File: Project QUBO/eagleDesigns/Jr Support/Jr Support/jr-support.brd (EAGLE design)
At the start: 242.6 x 96.8 mm, 254 parts, among them IC1 74LVC1G08DBV, IC2 TLC2272PW, IC3 74LVC1G08DBV, Q1 FDN5618P, U1 PCA9685, U2 LT3063, U3 LT3063

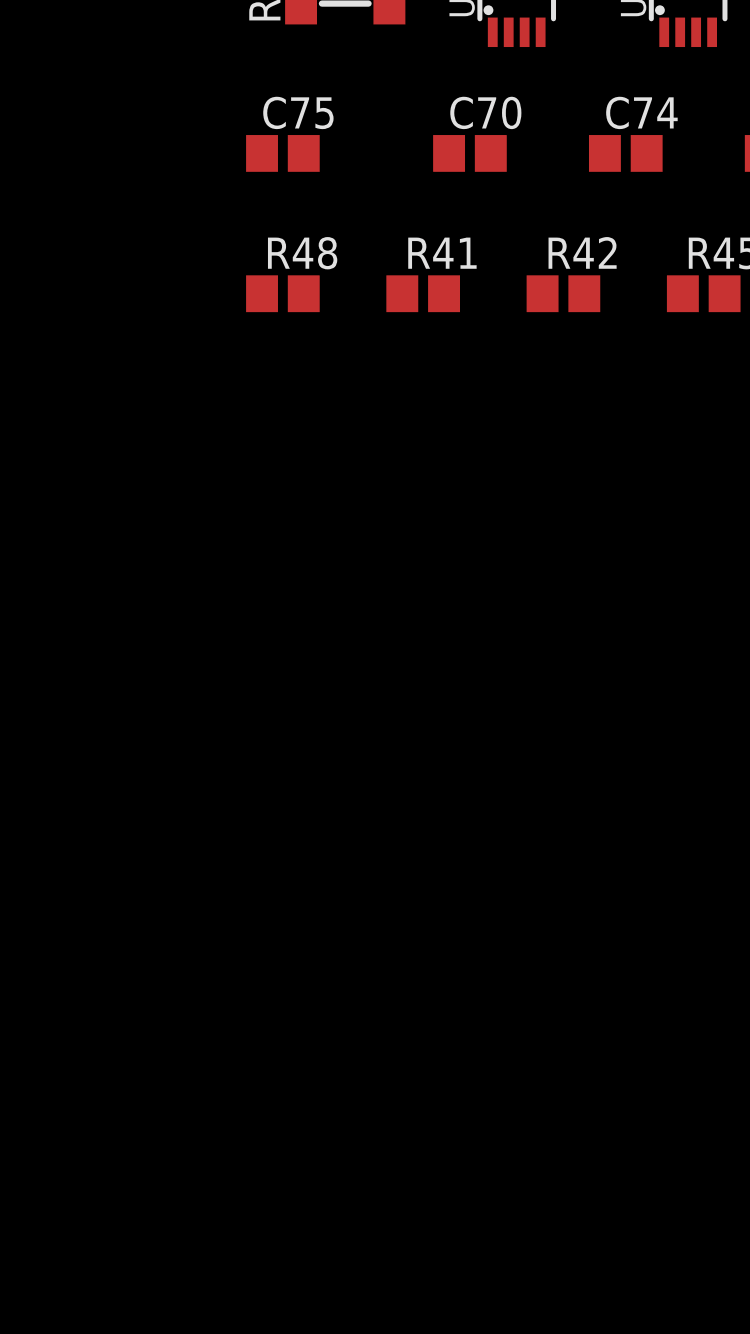
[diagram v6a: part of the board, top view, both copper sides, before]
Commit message: Created breadboards. Added 5V reg PG fault line.
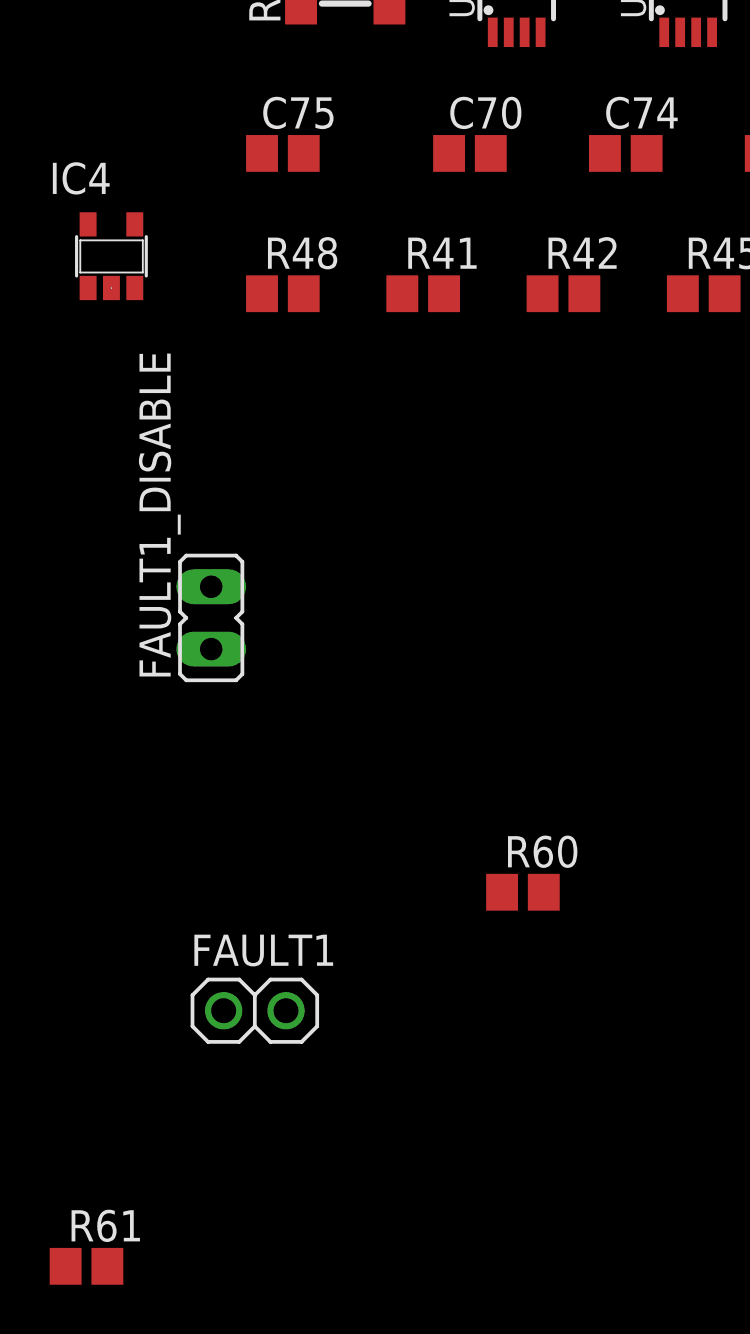
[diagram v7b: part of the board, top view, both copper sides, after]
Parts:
- added FAULT1: (no value), pinhead:1X02
- added FAULT1_DISABLE: (no value), jumper:JP1
- added IC4: 74LVC1G08DBV, 74xx-little-us:SOT23-5
- added R60: 1M, resistor:R0805
- added R61: 50k, resistor:R0805
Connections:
- new net 5V_PG: 5V_REG.19, IC4.2, R28.1, R61.1, U$58.P$2
- net +5V: now also FAULT1.1, FAULT1_DISABLE.2, R61.2
- net FAULT: now also IC4.4
- net GND: now also IC4.3, R60.1
- net N$76: now also FAULT1.2, FAULT1_DISABLE.1, IC4.1, R60.2; no longer 5V_REG.19, R28.1, U$58.P$2
- net VCC: now also IC4.5

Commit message: Updated VS pin on INA219s to 5V
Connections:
- net 5V: now also 12V_VOLTAGE.P$4, 5V_VOLTAGE.P$4, V-THRUST_VOLAGE.P$4
- net RELAY_OUT: no longer 12V_VOLTAGE.P$4, 5V_VOLTAGE.P$4, V-THRUST_VOLAGE.P$4
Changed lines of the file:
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@@
 <contactref element="C40" pad="1"/>
 <contactref element="5V_REG" pad="14"/>
-<contactref element="12V_VOLTAGE" pad="P$4"/>
-<contactref element="V-THRUST_VOLAGE" pad="P$4"/>
-<contactref element="5V_VOLTAGE" pad="P$4"/>
 <contactref element="12V_VOLTAGE" pad="P$8"/>
 <contactref element="V-THRUST_VOLAGE" pad="P$8"/>
@@
 <wire x1="63.795" y1="59.085" x2="55.245" y2="77.845" width="0" layer="19" extent="1-1"/>
 <wire x1="64.445" y1="59.085" x2="63.795" y2="59.085" width="0" layer="19" extent="1-1"/>
-<wire x1="65.745" y1="56.485" x2="64.445" y2="59.085" width="0" layer="19" extent="1-1"/>
-<wire x1="64.105" y1="38.395" x2="65.745" y2="56.485" width="0" layer="19" extent="1-1"/>
-<wire x1="53.34" y1="33.87" x2="64.105" y2="38.395" width="0" layer="19" extent="1-1"/>
-<wire x1="51.565" y1="33.905" x2="53.34" y2="33.87" width="0" layer="19" extent="1-1"/>
-<wire x1="51.565" y1="33.405" x2="51.565" y2="33.905" width="0" layer="19" extent="1-1"/>
-<wire x1="48.765" y1="33.405" x2="51.565" y2="33.405" width="0" layer="19" extent="1-1"/>
-<wire x1="46.99" y1="33.44" x2="48.765" y2="33.405" width="0" layer="19" extent="1-1"/>
-<wire x1="44.45" y1="33.44" x2="46.99" y2="33.44" width="0" layer="19" extent="1-1"/>
-<wire x1="45.72" y1="50.292" x2="46.99" y2="33.44" width="0" layer="19" extent="1-1"/>
+<wire x1="45.72" y1="50.292" x2="63.795" y2="59.085" width="0" layer="19" extent="1-1"/>
 <wire x1="34.595" y1="50.55" x2="45.72" y2="50.292" width="0" layer="19" extent="1-1"/>
 <wire x1="29.515" y1="50.55" x2="34.595" y2="50.55" width="0" layer="19" extent="1-1"/>
+<wire x1="46.99" y1="33.44" x2="45.72" y2="50.292" width="0" layer="19" extent="1-1"/>
+<wire x1="48.765" y1="33.405" x2="46.99" y2="33.44" width="0" layer="19" extent="1-1"/>
+<wire x1="44.45" y1="33.44" x2="46.99" y2="33.44" width="0" layer="19" extent="1-1"/>
+<wire x1="51.565" y1="33.405" x2="48.765" y2="33.405" width="0" layer="19" extent="1-1"/>
+<wire x1="51.565" y1="33.905" x2="51.565" y2="33.405" width="0" layer="19" extent="1-1"/>
+<wire x1="53.34" y1="33.87" x2="51.565" y2="33.905" width="0" layer="19" extent="1-1"/>
 <wire x1="45.72" y1="15.66" x2="46.99" y2="33.44" width="0" layer="19" extent="1-1"/>
 <wire x1="43.18" y1="15.66" x2="45.72" y2="15.66" width="0" layer="19" extent="1-1"/>
@@
 <wire x1="54.395" y1="12.065" x2="52.835" y2="13.085" width="0" layer="19" extent="1-1"/>
 <wire x1="58.715" y1="15.905" x2="54.395" y2="12.065" width="0" layer="19" extent="1-1"/>
-<wire x1="60.665" y1="13.305" x2="58.715" y2="15.905" width="0" layer="19" extent="1-1"/>
-<wire x1="99.98" y1="17.37" x2="60.665" y2="13.305" width="0" layer="19" extent="1-1"/>
+<wire x1="99.98" y1="17.37" x2="58.715" y2="15.905" width="0" layer="19" extent="1-1"/>
 <wire x1="107.53" y1="21.59" x2="99.98" y2="17.37" width="0" layer="19" extent="1-1"/>
-<wire x1="76.835" y1="-26.455" x2="60.665" y2="13.305" width="0" layer="19" extent="1-1"/>
+<wire x1="76.835" y1="-26.455" x2="54.395" y2="12.065" width="0" layer="19" extent="1-1"/>
 <wire x1="81.055" y1="-34.005" x2="76.835" y2="-26.455" width="0" layer="19" extent="1-1"/>
 <wire x1="-93.13" y1="139.7" x2="29.515" y2="50.55" width="0" layer="19" extent="1-1"/>
@@
 <wire x1="125.691359375" y1="62.858684375" x2="125.691359375" y2="62.776640625" width="0.4064" layer="16"/>
 <wire x1="125.691359375" y1="62.776640625" x2="125.73" y2="62.738" width="0.4064" layer="16"/>
-<wire x1="138.43" y1="63.715" x2="194.31" y2="52.07" width="0" layer="19" extent="1-1"/>
+<contactref element="12V_VOLTAGE" pad="P$4"/>
+<contactref element="V-THRUST_VOLAGE" pad="P$4"/>
+<contactref element="5V_VOLTAGE" pad="P$4"/>
+<wire x1="163.664" y1="57.912" x2="194.31" y2="52.07" width="0" layer="19" extent="1-1"/>
+<wire x1="163.164" y1="56.134" x2="163.664" y2="57.912" width="0" layer="19" extent="1-1"/>
+<wire x1="164.084" y1="62.23" x2="163.664" y2="57.912" width="0" layer="19" extent="1-1"/>
+<wire x1="162.814" y1="50.673" x2="163.164" y2="56.134" width="0" layer="19" extent="1-1"/>
+<wire x1="162.902" y1="46.228" x2="162.814" y2="50.673" width="0" layer="19" extent="1-1"/>
+<wire x1="162.656" y1="44.196" x2="162.902" y2="46.228" width="0" layer="19" extent="1-1"/>
+<wire x1="154.52" y1="57.912" x2="163.164" y2="56.134" width="0" layer="19" extent="1-1"/>
+<wire x1="154.02" y1="56.134" x2="154.52" y2="57.912" width="0" layer="19" extent="1-1"/>
+<wire x1="154.686" y1="62.23" x2="154.52" y2="57.912" width="0" layer="19" extent="1-1"/>
+<wire x1="145.288" y1="62.357" x2="154.686" y2="62.23" width="0" layer="19" extent="1-1"/>
+<wire x1="144.741" y1="58.039" x2="145.288" y2="62.357" width="0" layer="19" extent="1-1"/>
+<wire x1="144.114" y1="56.007" x2="144.741" y2="58.039" width="0" layer="19" extent="1-1"/>
+<wire x1="145.161" y1="51.943" x2="144.114" y2="56.007" width="0" layer="19" extent="1-1"/>
+<wire x1="144.868" y1="47.625" x2="145.161" y2="51.943" width="0" layer="19" extent="1-1"/>
+<wire x1="144.368" y1="45.847" x2="144.868" y2="47.625" width="0" layer="19" extent="1-1"/>
+<wire x1="138.43" y1="63.715" x2="145.288" y2="62.357" width="0" layer="19" extent="1-1"/>
 <wire x1="123.61" y1="60.96" x2="125.691359375" y2="62.776640625" width="0" layer="19" extent="1-16"/>
 <wire x1="109.64" y1="60.96" x2="120.65" y2="60.96" width="0" layer="19" extent="1-1"/>
@@
 <wire x1="115.785" y1="76.2" x2="105.15" y2="76.2" width="0" layer="19" extent="1-1"/>
 <wire x1="77.21" y1="76.2" x2="88.48" y2="76.2" width="0" layer="19" extent="1-1"/>
-<wire x1="154.686" y1="62.23" x2="133.6643375" y2="63.715" width="0" layer="19" extent="1-1"/>
-<wire x1="164.084" y1="62.23" x2="154.686" y2="62.23" width="0" layer="19" extent="1-1"/>
-<wire x1="145.288" y1="62.357" x2="154.686" y2="62.23" width="0" layer="19" extent="1-1"/>
-<wire x1="53.975" y1="83.445" x2="74.51" y2="76.2" width="0" layer="19" extent="1-1"/>
-<wire x1="54.3" y1="86.065" x2="53.975" y2="83.445" width="0" layer="19" extent="1-1"/>
-<wire x1="54.3" y1="90.465" x2="54.3" y2="86.065" width="0" layer="19" extent="1-1"/>
-<wire x1="54.95" y1="90.465" x2="54.3" y2="90.465" width="0" layer="19" extent="1-1"/>
-<wire x1="66.255" y1="36.195" x2="80.01" y2="60.96" width="0" layer="19" extent="1-1"/>
+<wire x1="65.745" y1="56.485" x2="80.01" y2="60.96" width="0" layer="19" extent="1-1"/>
+<wire x1="64.105" y1="38.395" x2="65.745" y2="56.485" width="0" layer="19" extent="1-1"/>
+<wire x1="66.255" y1="36.195" x2="64.105" y2="38.395" width="0" layer="19" extent="1-1"/>
 <wire x1="67.605" y1="32.695" x2="66.255" y2="36.195" width="0" layer="19" extent="1-1"/>
 <wire x1="67.605" y1="32.045" x2="67.605" y2="32.695" width="0" layer="19" extent="1-1"/>
@@
 <wire x1="67.605" y1="12.995" x2="71.12" y2="30.4927" width="0" layer="19" extent="1-1"/>
 <wire x1="63.5" y1="8.515" x2="67.605" y2="12.995" width="0" layer="19" extent="1-1"/>
+<wire x1="60.665" y1="13.305" x2="63.5" y2="8.515" width="0" layer="19" extent="1-1"/>
+<wire x1="53.975" y1="83.445" x2="74.51" y2="76.2" width="0" layer="19" extent="1-1"/>
+<wire x1="54.3" y1="86.065" x2="53.975" y2="83.445" width="0" layer="19" extent="1-1"/>
+<wire x1="54.3" y1="90.465" x2="54.3" y2="86.065" width="0" layer="19" extent="1-1"/>
+<wire x1="54.95" y1="90.465" x2="54.3" y2="90.465" width="0" layer="19" extent="1-1"/>
 <wire x1="73.04" y1="-38.245" x2="63.5" y2="8.515" width="0" layer="19" extent="1-1"/>
-<wire x1="145.161" y1="51.943" x2="194.31" y2="52.07" width="0" layer="19" extent="1-1"/>
-<wire x1="144.868" y1="47.625" x2="145.161" y2="51.943" width="0" layer="19" extent="1-1"/>
-<wire x1="144.368" y1="45.847" x2="144.868" y2="47.625" width="0" layer="19" extent="1-1"/>
 <wire x1="-20.74" y1="152.4" x2="54.3" y2="90.465" width="0" layer="19" extent="1-1"/>
 <wire x1="-16.09" y1="168.91" x2="-20.74" y2="152.4" width="0" layer="19" extent="1-1"/>
-<wire x1="154.02" y1="56.134" x2="-16.09" y2="168.91" width="0" layer="19" extent="1-1"/>
-<wire x1="162.656" y1="44.196" x2="154.02" y2="56.134" width="0" layer="19" extent="1-1"/>
-<wire x1="163.164" y1="56.134" x2="162.656" y2="44.196" width="0" layer="19" extent="1-1"/>
-<wire x1="-31.4" y1="168.91" x2="163.164" y2="56.134" width="0" layer="19" extent="1-1"/>
+<wire x1="-31.4" y1="168.91" x2="-16.09" y2="168.91" width="0" layer="19" extent="1-1"/>
 <wire x1="-42.33" y1="139.7" x2="-20.74" y2="152.4" width="0" layer="19" extent="1-1"/>
 <wire x1="-49.11" y1="146.05" x2="-42.33" y2="139.7" width="0" layer="19" extent="1-1"/>
@@
 <wire x1="-86.78" y1="139.7" x2="-80.43" y2="139.7" width="0" layer="19" extent="1-1"/>
 <wire x1="-99.48" y1="139.7" x2="-86.78" y2="139.7" width="0" layer="19" extent="1-1"/>
-<wire x1="154.52" y1="57.912" x2="-99.48" y2="139.7" width="0" layer="19" extent="1-1"/>
-<wire x1="163.664" y1="57.912" x2="154.52" y2="57.912" width="0" layer="19" extent="1-1"/>
-<wire x1="-127.85" y1="162.56" x2="163.664" y2="57.912" width="0" layer="19" extent="1-1"/>
-<wire x1="-137.58" y1="152.4" x2="-127.85" y2="162.56" width="0" layer="19" extent="1-1"/>
-<wire x1="-132.93" y1="139.7" x2="-137.58" y2="152.4" width="0" layer="19" extent="1-1"/>
-<wire x1="162.902" y1="46.228" x2="-80.43" y2="139.7" width="0" layer="19" extent="1-1"/>
-<wire x1="144.114" y1="56.007" x2="-42.33" y2="139.7" width="0" layer="19" extent="1-1"/>
-<wire x1="144.741" y1="58.039" x2="144.114" y2="56.007" width="0" layer="19" extent="1-1"/>
-<wire x1="162.814" y1="50.673" x2="144.741" y2="58.039" width="0" layer="19" extent="1-1"/>
+<wire x1="-132.93" y1="139.7" x2="-99.48" y2="139.7" width="0" layer="19" extent="1-1"/>
+<wire x1="-137.58" y1="152.4" x2="-132.93" y2="139.7" width="0" layer="19" extent="1-1"/>
+<wire x1="-127.85" y1="162.56" x2="-137.58" y2="152.4" width="0" layer="19" extent="1-1"/>
 </signal>
 <signal name="AIN11">
